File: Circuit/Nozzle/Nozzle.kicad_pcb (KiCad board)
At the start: 2 copper layers, 70 x 90.8 mm, 18 parts, among them J1 Coil Power, J2 CoilSignal, Q1 RFP30N06LE, U1 PC817

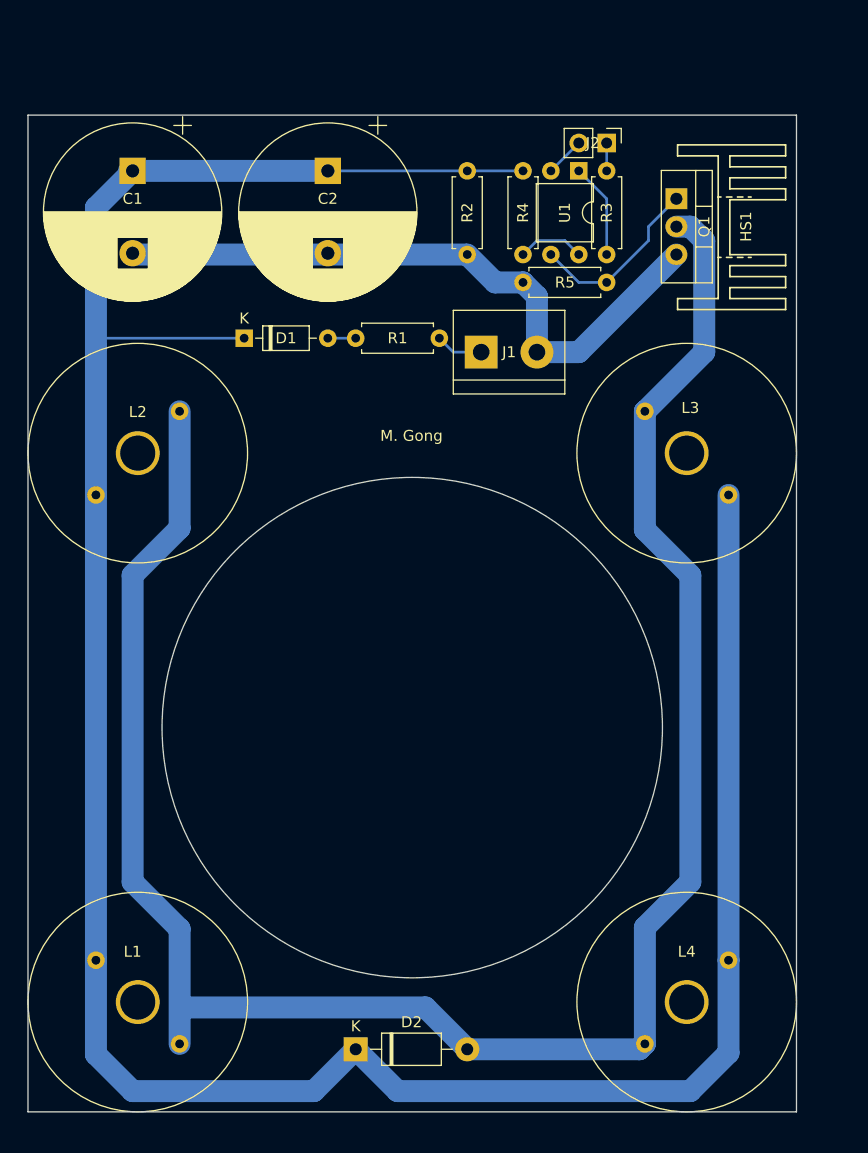
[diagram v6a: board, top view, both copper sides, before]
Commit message: [Circuit] Change the track width of nozzle module and switch module to allow larger current
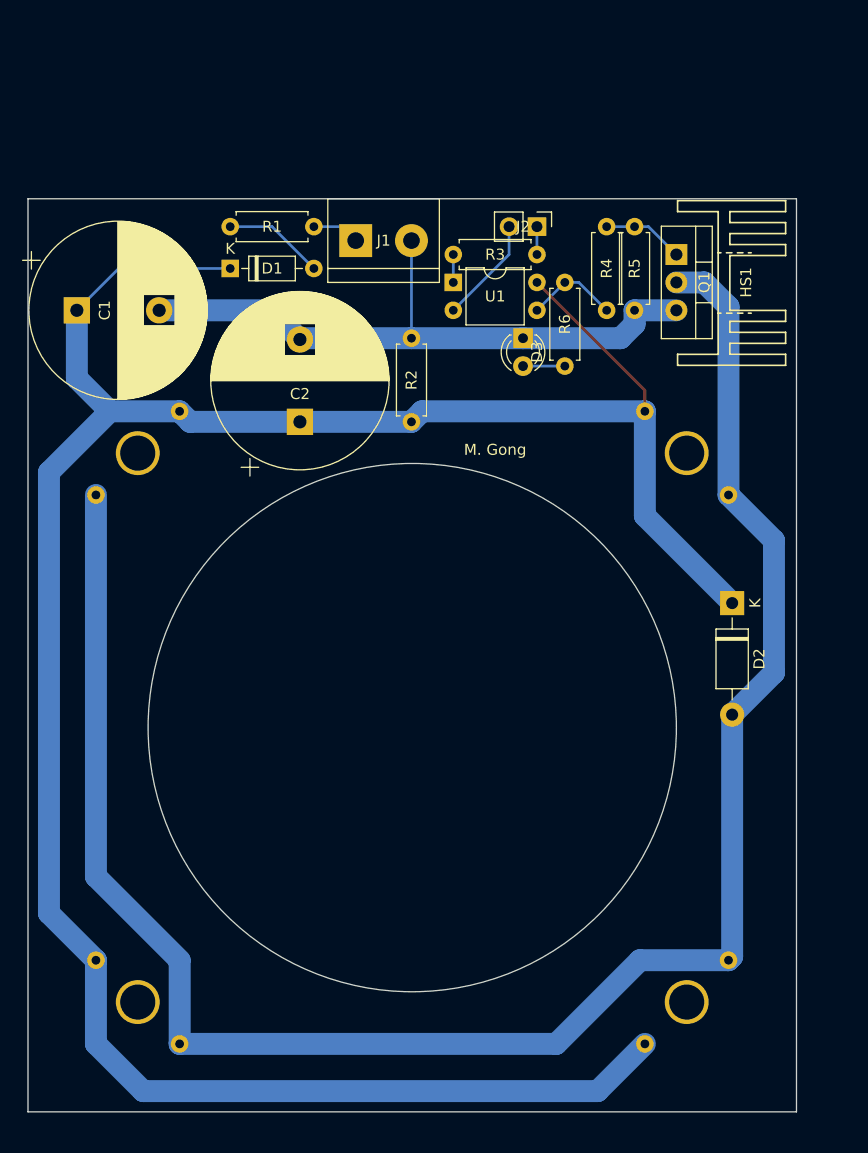
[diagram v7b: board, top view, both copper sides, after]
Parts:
- added D3: LED, LED_THT:LED_D3.0mm_FlatTop, F.Cu at (85.1, 49.5)
- added R4: 10K, Resistor_THT:R_Axial_DIN0207_L6.3mm_D2.5mm_P7.62mm_Horizontal, F.Cu at (92.7, 39.4)
- L1, L2, L3, L4: moved to B.Cu
- R6: renamed from R4; value 10K -> 2.2K
- moved D2 53.2 mm to (104.1, 73.7), turned to 270 degrees
- moved R2 23.4 mm to (74.9, 57.1), turned to 90 degrees
- moved C2 23.0 mm to (64.8, 57.1), turned to 90 degrees
- moved U1 15.3 mm to (78.7, 44.5), turned to 0 degrees
- moved J1 15.3 mm to (69.8, 40.6)
- moved R1 15.3 mm to (58.4, 39.4)
- moved R3 14.0 mm to (78.7, 41.9), turned to 0 degrees
- moved C1 13.7 mm to (44.5, 47.0), turned to 0 degrees
- moved R6 10.9 mm to (88.9, 44.5)
- moved J2 9.92 mm to (86.4, 39.4)
- moved D1 6.48 mm to (58.4, 43.2)
- moved R5 5.68 mm to (95.2, 39.4), turned to 270 degrees
- moved HS1 5.08 mm to (102.9, 44.5)
- moved Q1 5.08 mm to (99.1, 41.9)
- turned L1 to 0 degrees
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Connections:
- R6 pad 1: Net-(C1-Pad1) -> Net-(R4-Pad2)
- R6 pad 2: Net-(R4-Pad2) -> Net-(D3-Pad2)
- U1 pad 3: Net-(Q1-Pad1) -> Net-(R4-Pad2)
- U1 pad 4: Net-(R4-Pad2) -> Net-(C1-Pad1)
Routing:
- net Net-(C1-Pad1): track 246.0 -> 227.3 mm
- net Net-(D2-Pad2): track 186.8 -> 174.9 mm
- net Net-(Q1-Pad1): track 16.4 -> 7.40 mm
- net Net-(D1-Pad2): track 2.54 -> 9.20 mm
- net /CoilSignal-: track 3.59 -> 9.72 mm
- net Net-(R3-Pad1): track 8.67 -> 2.54 mm
- net Net-(D3-Pad2): track 0.00 -> 3.81 mm
- net Net-(R4-Pad2): track 6.13 -> 8.45 mm
- net /CoilPower-: track 59.8 -> 58.8 mm
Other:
- board size 70 x 90.8 mm -> 70 x 83.2 mm

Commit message: [Circuit] Optimize the pcb layout
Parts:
- moved R1 1.27 mm to (58.4, 40.6)
- moved R4 1.27 mm to (91.4, 39.4)
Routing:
- net Net-(Q1-Pad1): track 7.40 -> 8.67 mm
- net Net-(R4-Pad2): track 8.45 -> 7.18 mm
- net /CoilPower-: track 58.8 -> 58.0 mm
- net /CoilPower+: track 4.34 -> 3.81 mm
- net Net-(D1-Pad2): track 9.20 -> 8.67 mm
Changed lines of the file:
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@@
     (thickness 1.6)
     (drawings 6)
-    (tracks 59)
+    (tracks 56)
     (zones 0)
     (modules 20)
@@
   )
   (module Resistor_THT:R_Axial_DIN0207_L6.3mm_D2.5mm_P7.62mm_Horizontal (layer F.Cu)
-    (at 92.71 39.37 270)
+    (at 91.44 39.37 270)
     (descr "Resistor, Axial_DIN0207 series, Axial, Horizontal, pin pitch=7.62mm, 0.25W = 1/4W, length*diameter=6.3*2.5mm^2, http://cdn-reichelt.de/documents/datenblatt/B400/1_4W%23YAG.pdf")
     (tags "Resistor Axial_DIN0207 series Axial Horizontal pin pitch 7.62mm 0.25W = 1/4W length 6.3mm diameter 2.5mm")
@@
   )
   (module Resistor_THT:R_Axial_DIN0207_L6.3mm_D2.5mm_P7.62mm_Horizontal (layer F.Cu)
-    (at 58.42 39.37)
+    (at 58.42 40.64)
     (descr "Resistor, Axial_DIN0207 series, Axial, Horizontal, pin pitch=7.62mm, 0.25W = 1/4W, length*diameter=6.3*2.5mm^2, http://cdn-reichelt.de/documents/datenblatt/B400/1_4W%23YAG.pdf")
     (tags "Resistor Axial_DIN0207 series Axial Horizontal pin pitch 7.62mm 0.25W = 1/4W length 6.3mm diameter 2.5mm")
@@
   (gr_line (start 110 36.83) (end 110 120) (layer Edge.Cuts) (width 0.1))
   (gr_line (start 40 36.83) (end 110 36.83) (layer Edge.Cuts) (width 0.1))
-  (segment (start 68.58 39.37) (end 69.85 40.64) (width 0.25) (layer B.Cu) (net 1) (status 30))
-  (segment (start 66.04 39.37) (end 68.58 39.37) (width 0.25) (layer B.Cu) (net 1) (status 30))
+  (segment (start 66.04 40.64) (end 69.85 40.64) (width 0.25) (layer B.Cu) (net 1))
   (segment (start 62.11 46.99) (end 64.77 49.65) (width 2) (layer B.Cu) (net 2) (status 20))
   (segment (start 74.93 49.53) (end 64.89 49.53) (width 2) (layer B.Cu) (net 2) (status 30))
@@
   (segment (start 74.93 40.64) (end 74.93 49.53) (width 0.25) (layer B.Cu) (net 2) (status 30))
   (segment (start 85.09 49.53) (end 74.93 49.53) (width 2) (layer B.Cu) (net 2) (status 30))
-  (segment (start 99.06 46.99) (end 95.25 46.99) (width 2) (layer B.Cu) (net 2))
-  (segment (start 95.25 46.99) (end 95.25 48.26) (width 2) (layer B.Cu) (net 2))
-  (segment (start 93.98 49.53) (end 85.09 49.53) (width 2) (layer B.Cu) (net 2))
-  (segment (start 95.25 48.26) (end 93.98 49.53) (width 2) (layer B.Cu) (net 2))
-  (segment (start 62.23 39.37) (end 66.04 43.18) (width 0.25) (layer B.Cu) (net 3) (status 20))
-  (segment (start 58.42 39.37) (end 62.23 39.37) (width 0.25) (layer B.Cu) (net 3) (status 10))
-  (segment (start 92.71 39.37) (end 95.25 39.37) (width 0.25) (layer B.Cu) (net 4))
-  (segment (start 96.52 39.37) (end 99.06 41.91) (width 0.25) (layer B.Cu) (net 4))
-  (segment (start 95.25 39.37) (end 96.52 39.37) (width 0.25) (layer B.Cu) (net 4))
+  (segment (start 99.06 46.99) (end 95.25 46.99) (width 2) (layer B.Cu) (net 2) (status 30))
+  (segment (start 95.25 46.99) (end 92.71 49.53) (width 2) (layer B.Cu) (net 2) (status 10))
+  (segment (start 92.71 49.53) (end 85.09 49.53) (width 2) (layer B.Cu) (net 2) (status 20))
+  (segment (start 63.5 40.64) (end 66.04 43.18) (width 0.25) (layer B.Cu) (net 3))
+  (segment (start 58.42 40.64) (end 63.5 40.64) (width 0.25) (layer B.Cu) (net 3))
+  (segment (start 91.44 39.37) (end 95.25 39.37) (width 0.25) (layer B.Cu) (net 4) (status 30))
+  (segment (start 96.52 39.37) (end 99.06 41.91) (width 0.25) (layer B.Cu) (net 4) (status 20))
+  (segment (start 95.25 39.37) (end 96.52 39.37) (width 0.25) (layer B.Cu) (net 4) (status 10))
   (segment (start 83.82 41.91) (end 78.74 46.99) (width 0.25) (layer B.Cu) (net 5) (status 20))
   (segment (start 83.82 41.91) (end 83.82 39.37) (width 0.25) (layer B.Cu) (net 5) (status 20))
@@
   (segment (start 104.14 83.82) (end 104.14 105.86) (width 2) (layer B.Cu) (net 8) (status 30))
   (segment (start 78.74 41.91) (end 78.74 44.45) (width 0.25) (layer B.Cu) (net 9) (status 30))
-  (segment (start 90.17 44.45) (end 92.71 46.99) (width 0.25) (layer B.Cu) (net 10) (status 20))
   (segment (start 86.36 46.99) (end 88.9 44.45) (width 0.25) (layer B.Cu) (net 10) (status 30))
-  (segment (start 88.9 44.45) (end 90.17 44.45) (width 0.25) (layer B.Cu) (net 10) (status 10))
+  (segment (start 88.9 44.45) (end 91.44 46.99) (width 0.25) (layer B.Cu) (net 10) (status 30))
   (segment (start 85.09 52.07) (end 88.9 52.07) (width 0.25) (layer B.Cu) (net 11) (status 30))
 )
